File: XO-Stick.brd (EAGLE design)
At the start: 105.4 x 54.1 mm, 29 parts, among them J1 POWER, SW1 USER, U1 TINY85P, U2 TINY861A, U3 ARDUINO-SHIELD, X1 USBPCB, X2 USBMINIB

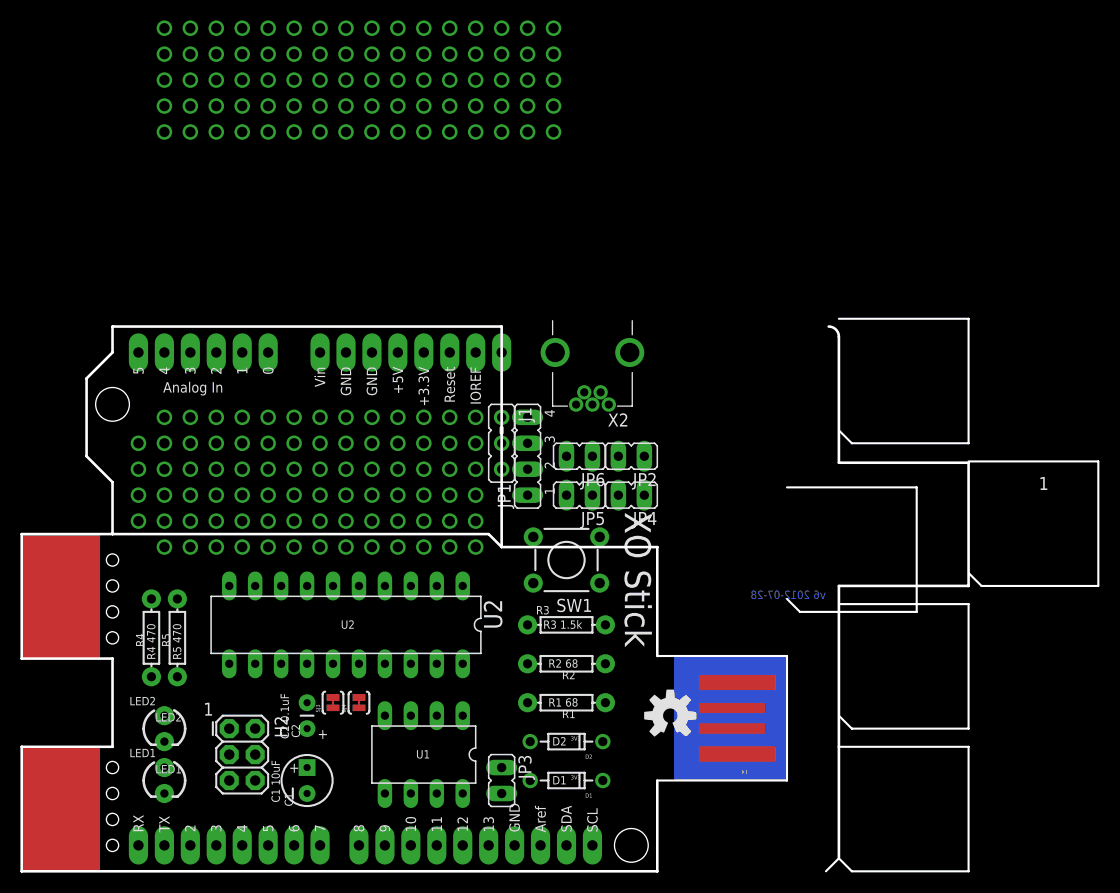
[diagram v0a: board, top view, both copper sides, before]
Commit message: v7 of board/schematic.  Fixed remaining issues with v6. 2-layer routing.
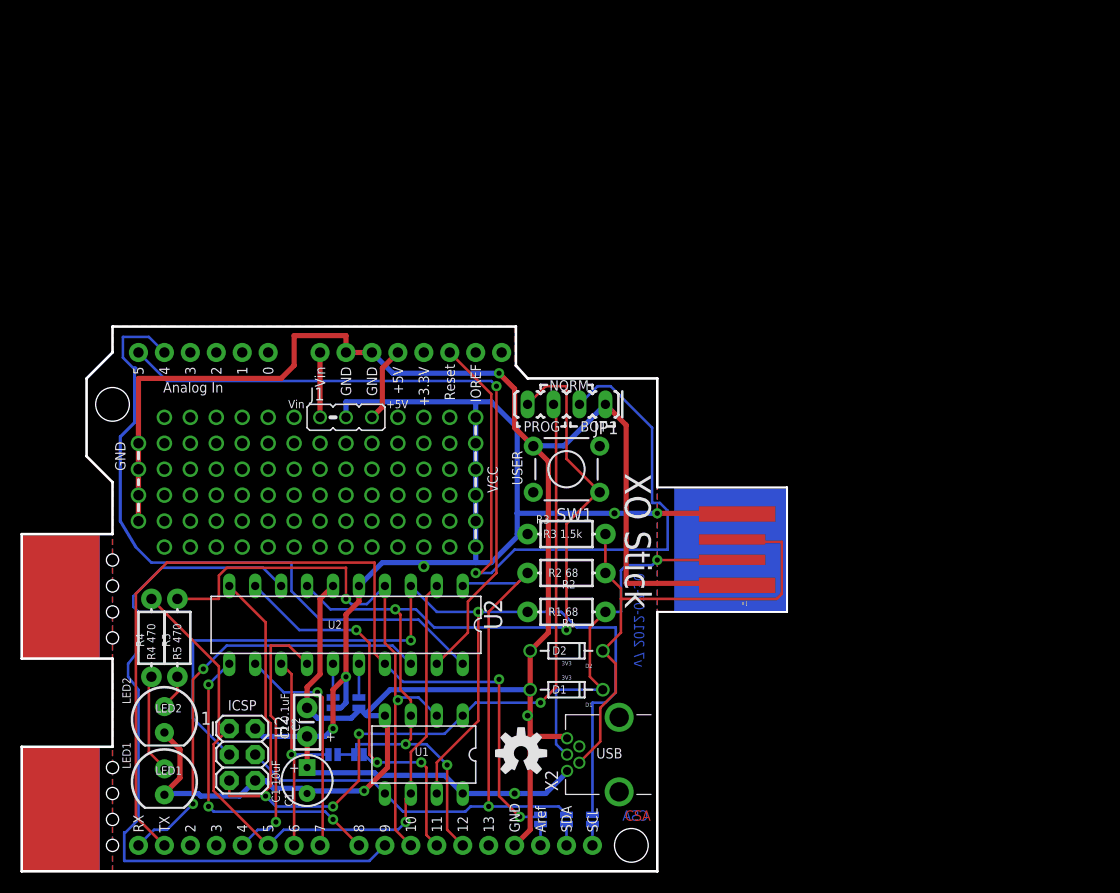
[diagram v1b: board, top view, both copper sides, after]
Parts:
- removed JP2: 85MOTR, jumper:JP1
- removed JP3: REF, jumper:JP1
- removed JP4: SDA, jumper:JP1
- removed JP5: SCL, jumper:JP1
- removed JP6: 85MOTL, jumper:JP1
- removed SJ3: AVCC (N/C), SparkFun:SJ_2S-TRACE
- removed SJ4: AGND (N/C), SparkFun:SJ_2S-TRACE
- added J2: 85MOTR, xorduino:SJ-2S-NO
- added J3: 85MOTL, xorduino:SJ-2S-NO
- added J4: REF, xorduino:SJ-2S-NO
- added J5: SCL, xorduino:SJ-2S-NO
- added J6: SDA, xorduino:SJ-2S-NO
- added J7: AVCC (N/C), xorduino:SJ-2S-BOT-TRACE-NOCONFLICT
- added J8: AGND (N/C), xorduino:SJ-2S-BOT-TRACE-NOCONFLICT
- C2: device SparkFun:CAP-PTH-SMALL -> SparkFun-Passives:CAP-PTH-SMALL-KIT
- JP1: device jumper:JP4 -> xorduino:JP4
- LED1, LED2: device SparkFun:LED3MM -> xorduino:LED3MM-KIT
- R1, R2, R3, R4, R5: device SparkFun:AXIAL-0.3 -> SparkFun-Passives:AXIAL-0.3-KIT
- moved X2 39.5 mm to (58.5, 11.4), turned to 180 degrees
- moved X1 16.5 mm to (69.8, 31.5)
- moved J1 15.5 mm to (31.8, 44.5), turned to 0 degrees
- moved U$1 15.1 mm to (48.9, 11.6)
- moved R3 8.89 mm to (53.3, 33.0)
- moved D1 8.89 mm to (53.3, 17.8)
- moved D2 8.89 mm to (53.3, 21.6)
- moved R2 8.89 mm to (53.3, 29.2)
- moved R1 8.89 mm to (53.3, 25.4)
- moved SW1 8.89 mm to (53.3, 39.4)
- moved JP1 6.35 mm to (53.3, 45.7), turned to 180 degrees
- moved LED2 0.89 mm to (14.0, 14.9)
- moved C2 0.63 mm to (27.9, 14.6)
- moved LED1 0.13 mm to (14.0, 8.76)
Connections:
- net N$1 renamed ARD_VIN
- net N$2 renamed ARD_5V
- net USB-D+ renamed USB-D_P
- net USB-D- renamed USB-D_M
- removed net D+: H2.3, JP5.2, R1.P$2, U1.7, U2.3
- removed net D-: H2.4, JP4.2, R2.P$2, U1.5, U2.1
- new net D_M: H2.4, J6.2, R2.P$2, U1.5, U2.1
- new net D_P: H2.3, J5.2, R1.P$2, U1.7, U2.3
- net AGND: now also J8.2; no longer SJ4.2
- net AREF: now also J4.2; no longer JP3.2
- net AVCC: now also J7.2; no longer SJ3.2
- net D4: now also J2.2, J3.1; no longer JP2.2, JP6.1
- net GND: now also J8.1; no longer SJ4.1
- net PA3: now also J4.1; no longer JP3.1
- net PA5: now also J2.1; no longer JP2.1
- net PB6: now also J3.2; no longer JP6.2
- net SCL: now also J5.1; no longer JP5.1
- net SDA: now also J6.1; no longer JP4.1
- net VCC: now also J7.1; no longer SJ3.1
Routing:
- net GND: track 0.00 -> 222.6 mm, vias 0 -> 7
- net VCC: track 0.00 -> 144.6 mm, vias 0 -> 12
- net D_P: track 0.00 -> 100.6 mm, vias 0 -> 2
- net D4: track 0.00 -> 93.5 mm, vias 0 -> 4
- net RST: track 0.00 -> 91.8 mm, vias 0 -> 4
- net PA3: track 0.00 -> 89.3 mm, vias 0 -> 2
- net PB5: track 0.00 -> 70.0 mm
- net D1: track 0.00 -> 69.5 mm, vias 0 -> 1
- net ARD_RST: track 0.00 -> 66.5 mm, vias 0 -> 1
- net PA1: track 0.00 -> 66.0 mm, vias 0 -> 1
- net PA0: track 0.00 -> 65.4 mm
- net D_M: track 0.00 -> 64.7 mm, vias 0 -> 1
- net D3: track 0.00 -> 58.3 mm, vias 0 -> 2
- net USB-D_M: track 0.00 -> 51.9 mm
- net PA2: track 0.00 -> 42.6 mm, vias 0 -> 2
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- added copper zone on layer 16, net GND
- added copper zone on layer 2, net GND
- added copper zone on layer 1, net VCC
- added copper zone on layer 15, net VCC
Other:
- board size 105.4 x 54.1 mm -> 74.9 x 53.3 mm
- board text added: "+5V"
- board text added: "AREF/PA3"
- board text added: "BOT"
- board text added: "CSA"
- board text added: "GND"
- board text added: "ICSP"
- board text added: "L"
- board text added: "N/C"
- board text added: "NORM"
- board text added: "PA0"
- board text added: "PA1"
- board text added: "PA2"
- board text added: "PA3"
- board text added: "PA4"
- board text added: "PA5"
- board text added: "PA6"
- board text added: "PA7"
- board text added: "PB1"
- board text added: "PB3"
- board text added: "PB4"
- board text added: "PB4->MOTORS"
- board text added: "PB5"
- board text added: "PB6"
- board text added: "PB7"
- board text added: "PROG"
- board text added: "R"
- board text added: "RST"
- board text added: "Reset"
- board text added: "SCL/PB2"
- board text added: "SDA/PB0"
- board text added: "USB"
- board text added: "USER"
- board text added: "VCC"
- board text added: "Vin"
- board text added: "v7 2012-07-30"
- board text removed: "v6 2012-07-28"

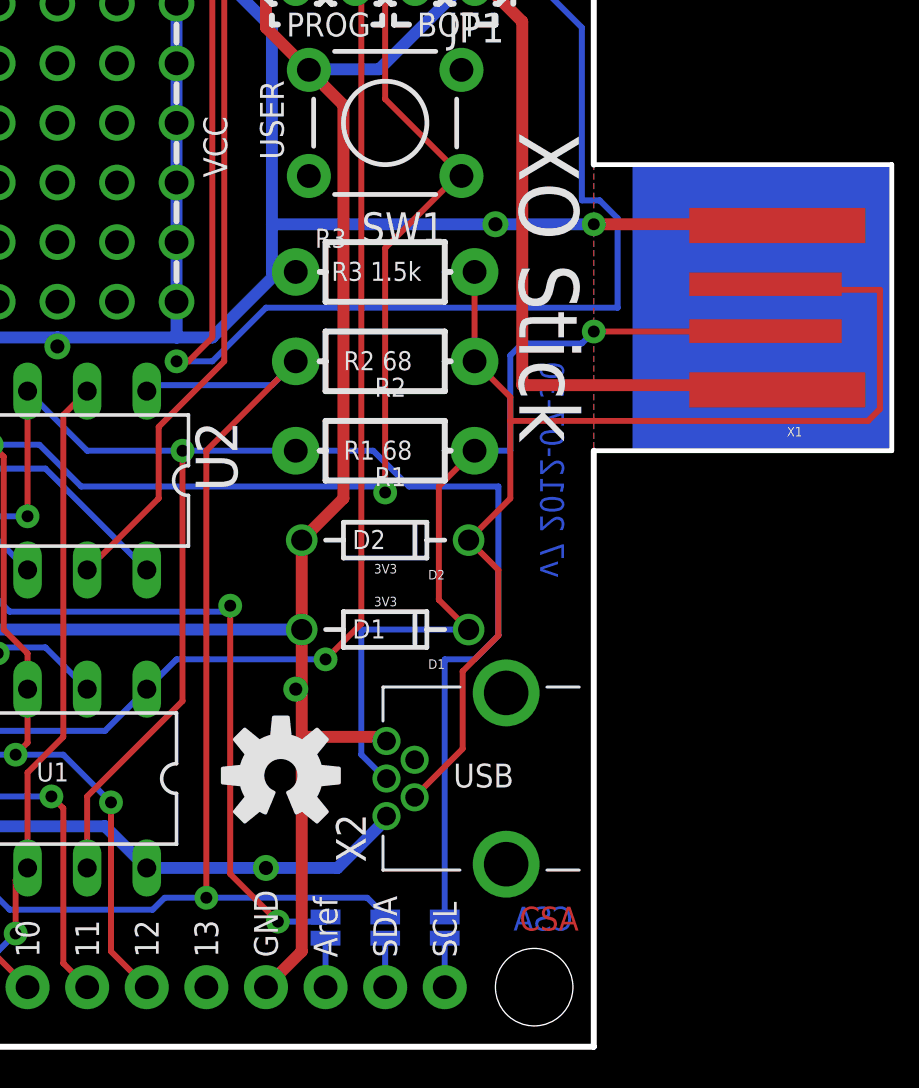
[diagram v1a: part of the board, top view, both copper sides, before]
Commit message: XO Stick v8: add jumper between VBUS and VCC; make SDA/SCL jumpers N/C.
SDA and SCL jumpers need to be closed in order to program XO Stick from
an XOrduino. Splitting VBUS from VCC is needed in order to make a 3.3v
variant XO Stick for XO unbricking.
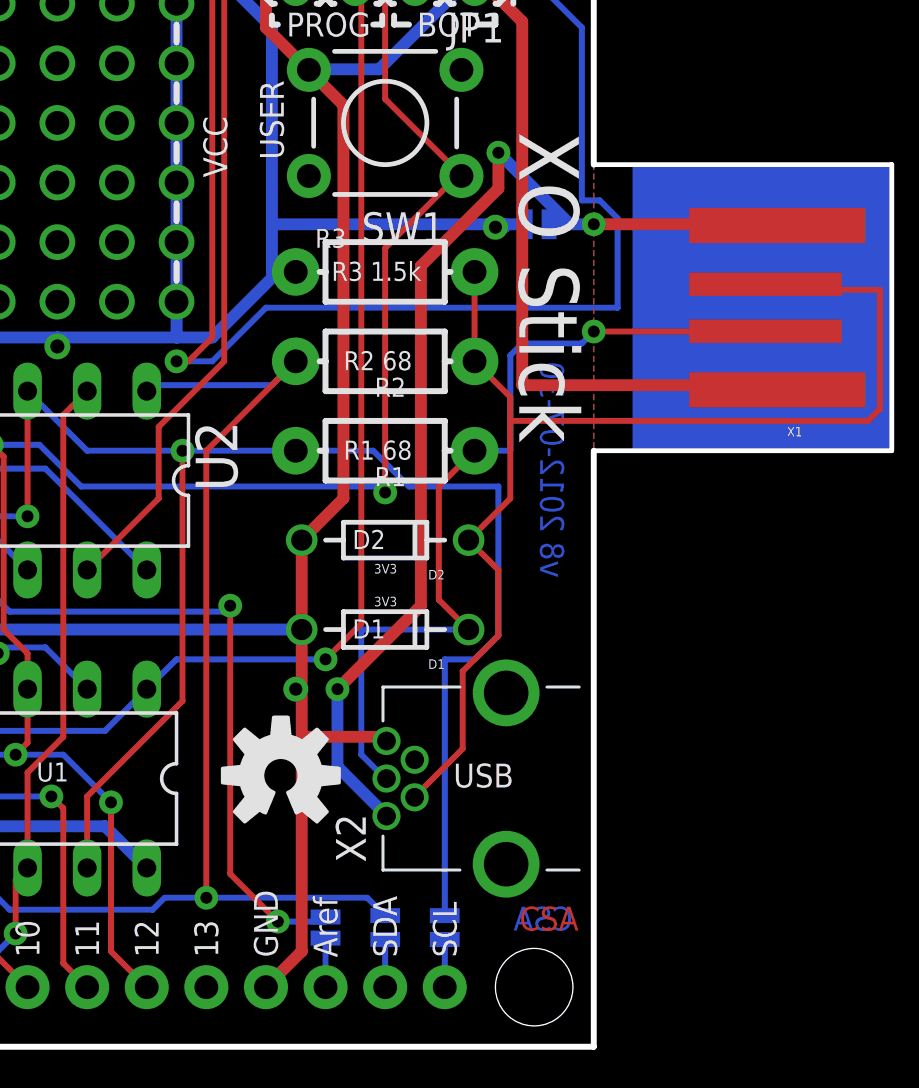
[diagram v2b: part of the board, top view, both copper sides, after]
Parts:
- added J9: EXT VCC, xorduino:SJ-2S-BOT-TRACE-NOCONFLICT-PAD
- J5, J6: device xorduino:SJ-2S-NO -> xorduino:SJ-2S-BOT-TRACE-NOCONFLICT-PAD
- flipped J5 to the top
- flipped J6 to the top
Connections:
- new net VBUS: J9.1, X1.5V, X2.VBUS
- net VCC: now also J9.2; no longer X1.5V, X2.VBUS
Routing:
- net VBUS: track 0.00 -> 46.0 mm, vias 0 -> 3
- net VCC: track 144.6 -> 123.2 mm, vias 12 -> 10
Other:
- board text added: "VBUS"
- board text added: "v8 2012-07-30"
- board text removed: "v7 2012-07-30"

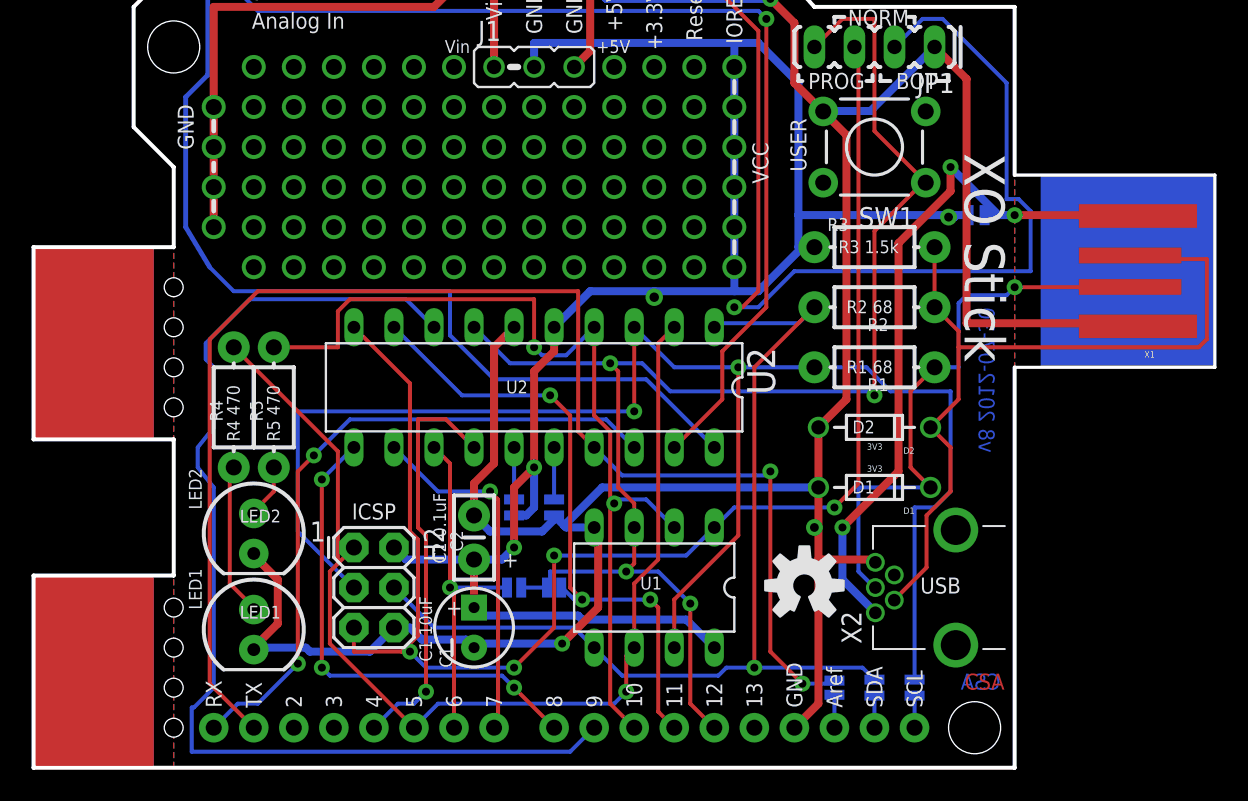
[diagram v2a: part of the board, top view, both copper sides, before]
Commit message: XO Stick v9: add silkscreen to break-off tabs, move some traces.
Moved traces away from break-off tabs and removed one trace from the
top side of the USB connector.
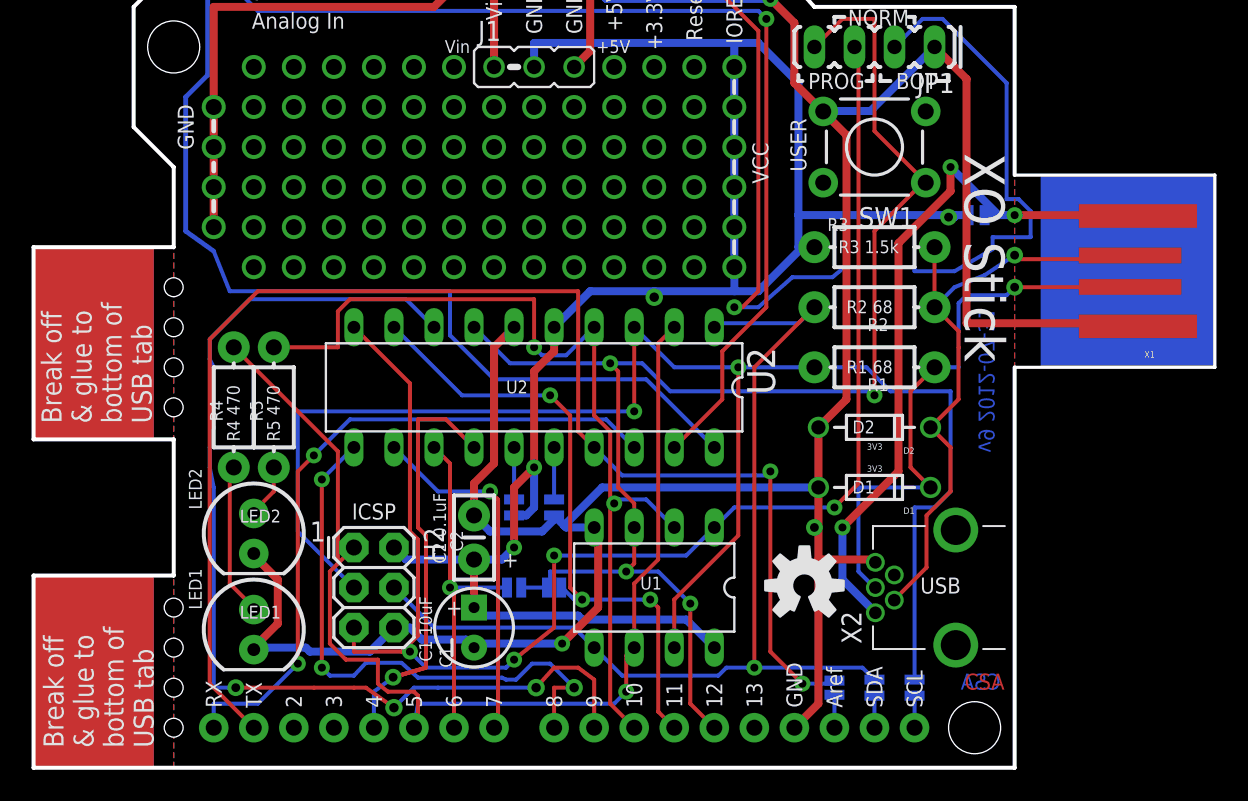
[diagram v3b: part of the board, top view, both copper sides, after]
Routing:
- net USB-D_M: track 51.9 -> 39.6 mm, vias 0 -> 1
- net PA7: track 31.1 -> 36.6 mm
- net D1: track 69.5 -> 72.6 mm
- net PB5: track 70.0 -> 67.2 mm, vias 0 -> 3
- net PA4: track 26.0 -> 28.4 mm
- net PA2: track 42.6 -> 43.5 mm
- net ARD_RST: track 66.5 -> 65.7 mm
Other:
- board text added: "& glue to"
- board text added: "Bottom"
- board text added: "Break off"
- board text added: "USB tab"
- board text added: "bottom of"
- board text added: "v9 2012-07-31"
- board text removed: "v8 2012-07-30"

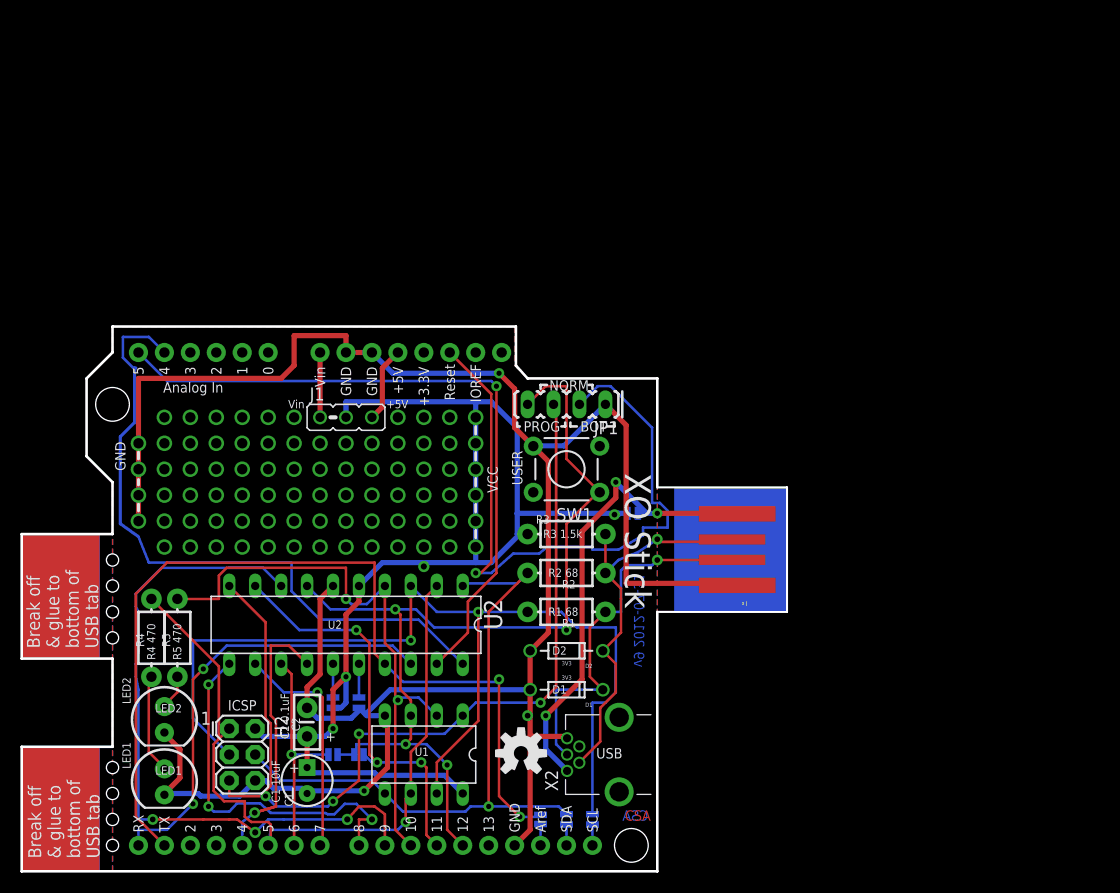
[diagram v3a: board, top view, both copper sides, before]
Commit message: XO Stick v10: moved USB connector up 10 mil to better fit vertical XO port.
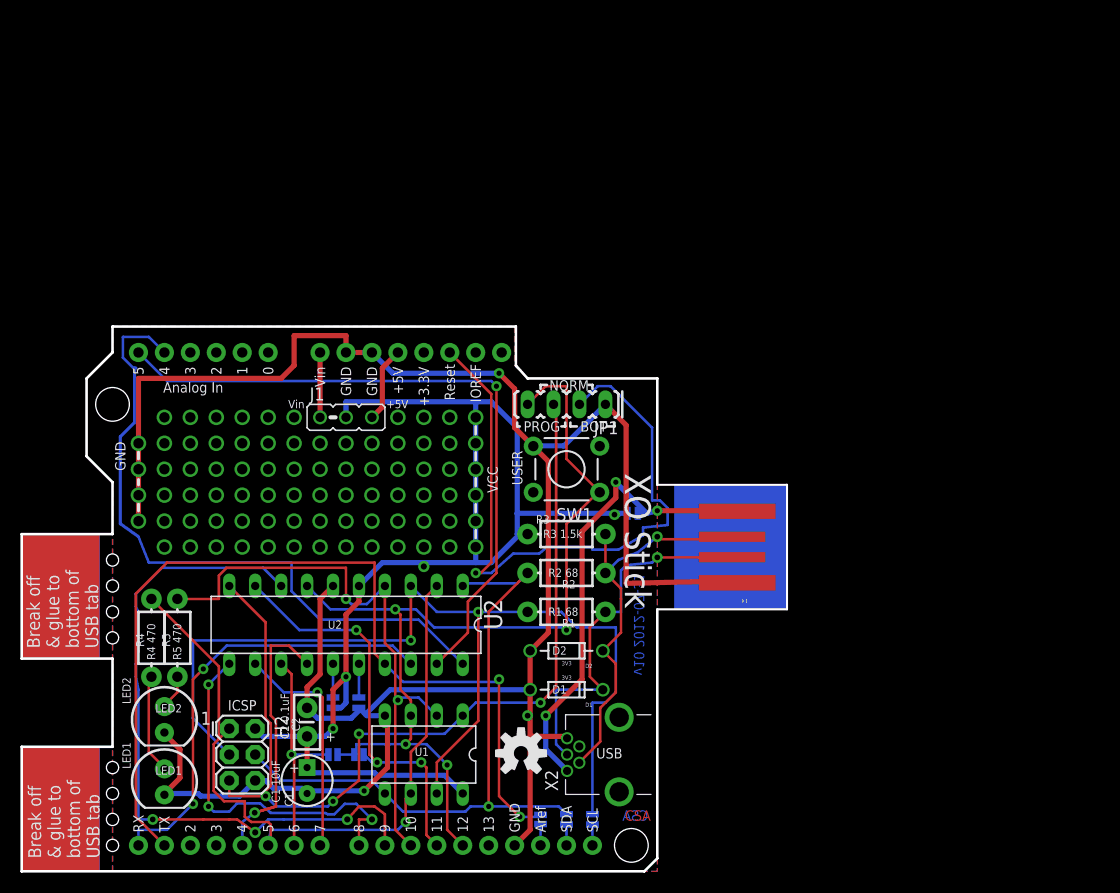
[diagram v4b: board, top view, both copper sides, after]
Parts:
- moved X1 0.25 mm to (69.8, 31.8)
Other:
- outline, holes or cut-outs redrawn
- board text added: "v10 2012-07-31"
- board text removed: "v9 2012-07-31"
